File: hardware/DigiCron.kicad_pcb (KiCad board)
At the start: 2 copper layers, 36 x 36 mm, 57 parts, among them J100 Solder pad, J101 Solder pad, J102 Solder pad, J103 Solder pad, J200 Conn_Receptacle_2P, J201 Solder pad, J202 Solder pad, J203 Solder pad, J204 Solder pad, Q100 BSS138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

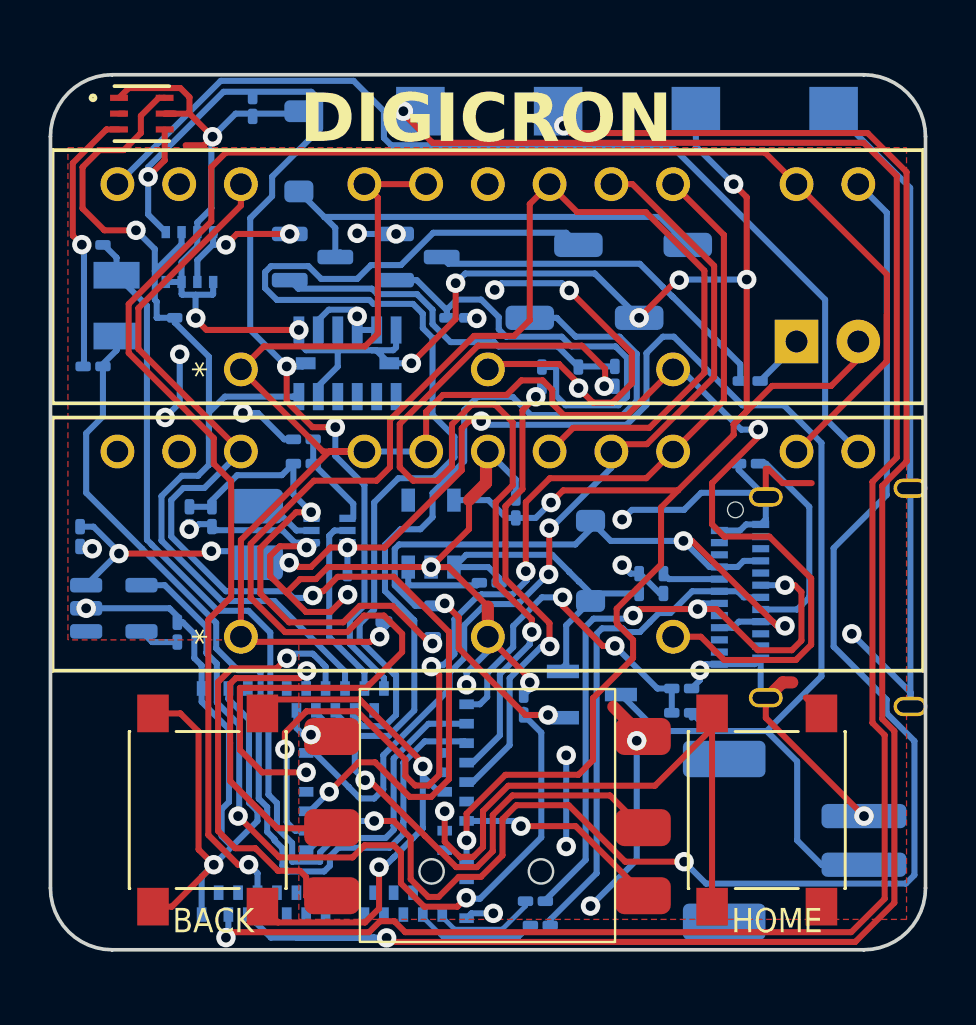
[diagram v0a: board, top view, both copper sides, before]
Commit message: Add mounting tabs to edges of PCB
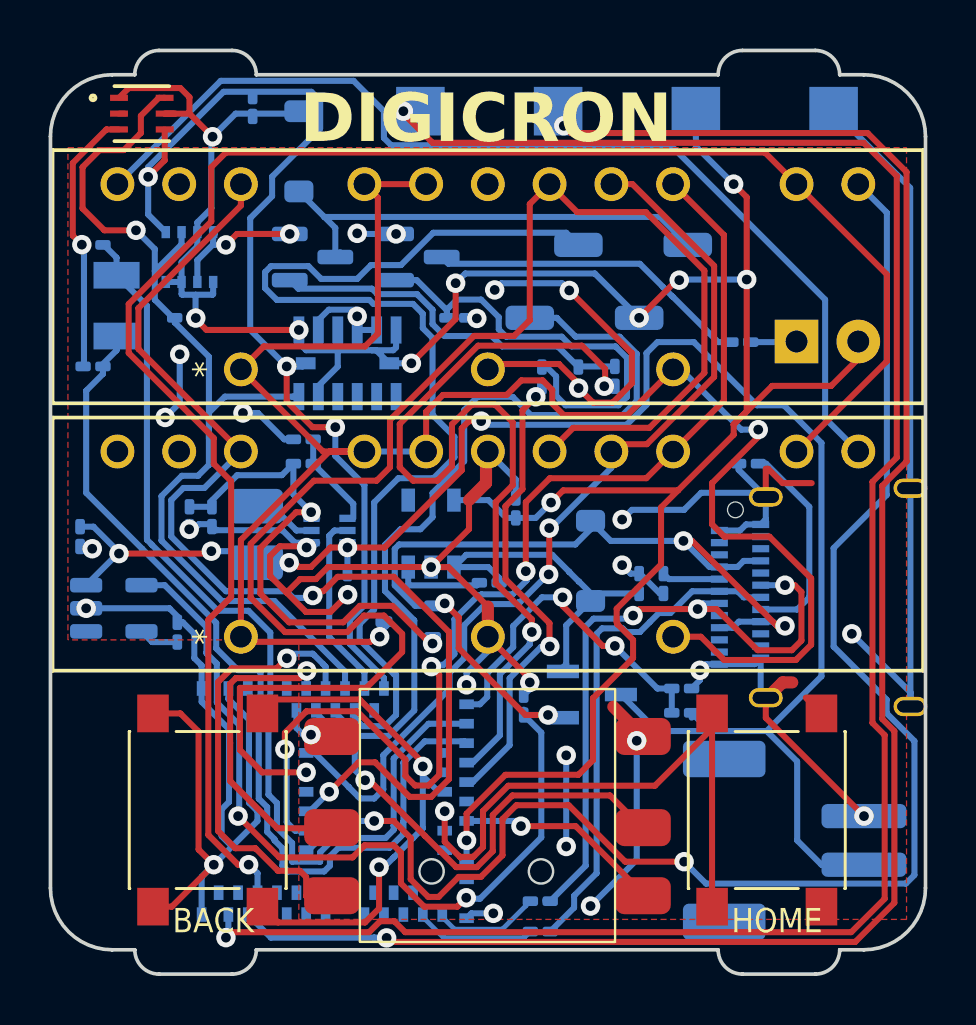
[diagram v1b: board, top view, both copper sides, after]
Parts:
- moved R100 1.65 mm to (208.3, 77.0)
- moved R209 0.25 mm to (200.1, 101.3)
- moved R210 0.20 mm to (200.1, 100.0)
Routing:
- net SWDIO: track 76.5 -> 73.3 mm
- net HCMS_RS: track 75.4 -> 73.4 mm
- net Net-(Q100-D): track 14.8 -> 13.4 mm
- net +3V3: track 109.9 -> 108.7 mm
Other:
- board size 36 x 36 mm -> 36 x 38 mm
- board text added: "V1"

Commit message: Generate Gerber files
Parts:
- moved C200 58.2 mm to (148.8, 105.0)
- moved C202 58.2 mm to (136.8, 105.0)
- moved C203 58.2 mm to (130.3, 102.3)
- moved C205 58.2 mm to (125.8, 103.1)
- moved C206 58.2 mm to (126.3, 91.1)
- moved C207 58.2 mm to (126.3, 96.1)
- moved D100 58.2 mm to (155.3, 95.1)
- moved D101 58.2 mm to (134.8, 87.3)
- moved D200 58.2 mm to (146.8, 104.1)
- moved D201 58.2 mm to (139.3, 106.6)
- moved J100 58.2 mm to (150.8, 91.1)
- moved J101 58.2 mm to (148.8, 94.1)
- moved J102 58.2 mm to (146.3, 91.1)
- moved J103 58.2 mm to (144.3, 94.1)
- moved J200 58.2 mm to (155.2, 115.6)
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
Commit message: Make minor alterations to not use custom font on PCB
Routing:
- net GND: track 192.8 -> 199.8 mm
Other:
- board text removed: "DIGICRON"

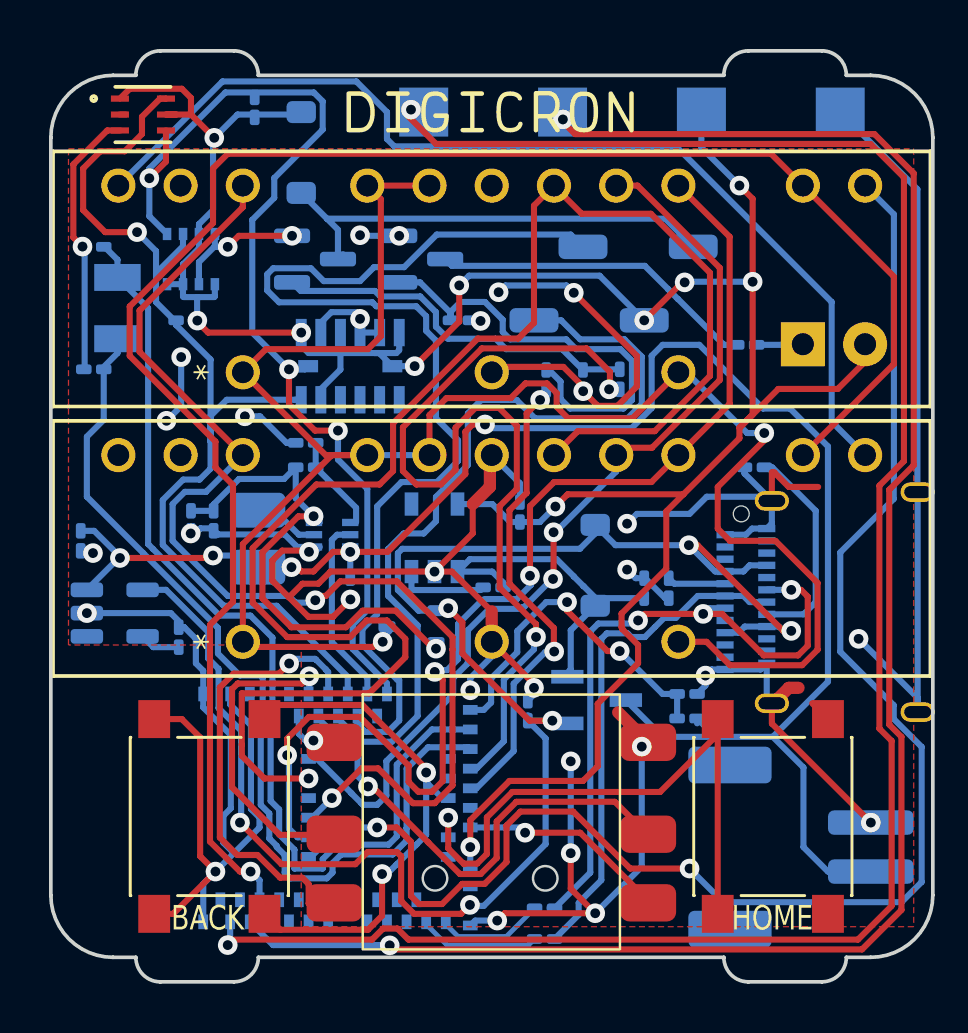
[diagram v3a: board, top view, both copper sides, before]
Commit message: Update PCB to use 0402 resistor/capacitor packages
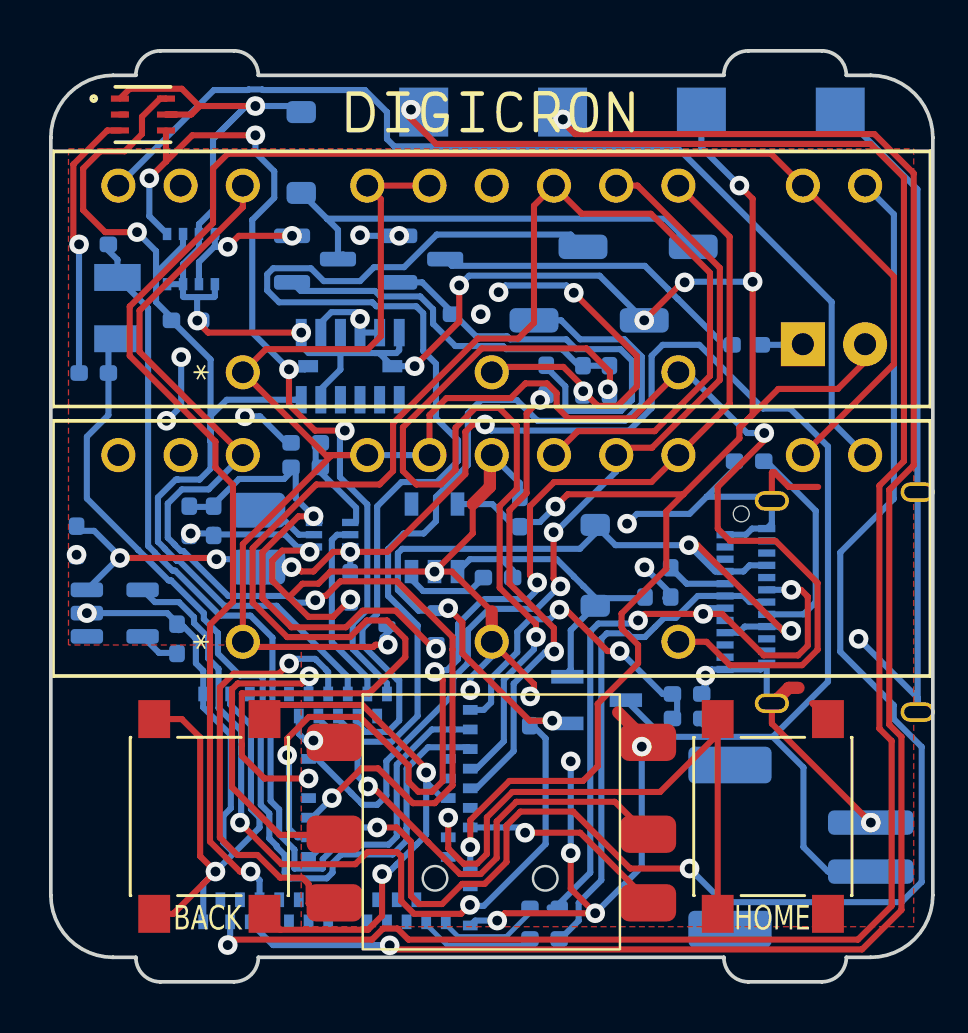
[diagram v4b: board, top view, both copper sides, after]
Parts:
- C200, C201, C202, C203, C204, C205, C206, C207, R100, R101, R102, R103, R104, R106, R107: footprint Capacitor_SMD:C_0201_0603Metric_Pad0.64x0.40mm_HandSolder -> Resistor_SMD:R_0402_1005Metric_Pad0.72x0.64mm_HandSolder
- R200, R201, R202, R203, R204, R205, R206, R207, R208, R209, R210: footprint Resistor_SMD:R_0201_0603Metric_Pad0.64x0.40mm_HandSolder -> Resistor_SMD:R_0402_1005Metric_Pad0.72x0.64mm_HandSolder
- moved R107 0.54 mm to (132.9, 86.0), turned to -90 degrees
- moved R203 0.45 mm to (142.8, 104.6)
- moved R103 0.42 mm to (147.4, 96.6)
- moved R102 0.34 mm to (141.5, 93.9)
- moved R201 0.33 mm to (153.1, 99.9)
- moved R200 0.25 mm to (149.9, 104.8)
- moved C200 0.24 mm to (148.8, 104.8)
- moved C205 0.17 mm to (125.6, 103.1)
- moved C207 0.15 mm to (126.3, 96.3)
- moved C206 0.10 mm to (126.3, 91.0)
- moved R208 0.10 mm to (129.7, 107.1)
- moved R202 0.08 mm to (144.1, 110.1)
- moved C203 0.07 mm to (130.2, 102.3)
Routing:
- net SCL: track 43.4 -> 37.0 mm, vias 3 -> 4
- net +3V3: track 108.7 -> 112.3 mm
- net Net-(D200-K): track 14.6 -> 13.2 mm
- net Net-(Q100-G): track 18.4 -> 17.4 mm
- net HCMS_CLOCK: track 47.2 -> 48.0 mm
- net VBAT: track 70.9 -> 71.4 mm

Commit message: Fix a few resistor values on PCB relating to power management
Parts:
- R205: value 732K -> 100K
- R206: value 100K -> 10K
- R207: value 100K -> 5.1K
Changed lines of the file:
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@@
 			)
 		)
-		(property "Value" "732K"
+		(property "Value" "100K"
 			(at 0 -1.17 0)
 			(layer "B.Fab")
@@
 			)
 		)
-		(property "Value" "100K"
+		(property "Value" "10K"
 			(at 0 -1.17 0)
 			(layer "B.Fab")
@@
 			)
 		)
-		(property "Value" "100K"
+		(property "Value" "5.1K"
 			(at 0 -1.17 180)
 			(layer "B.Fab")

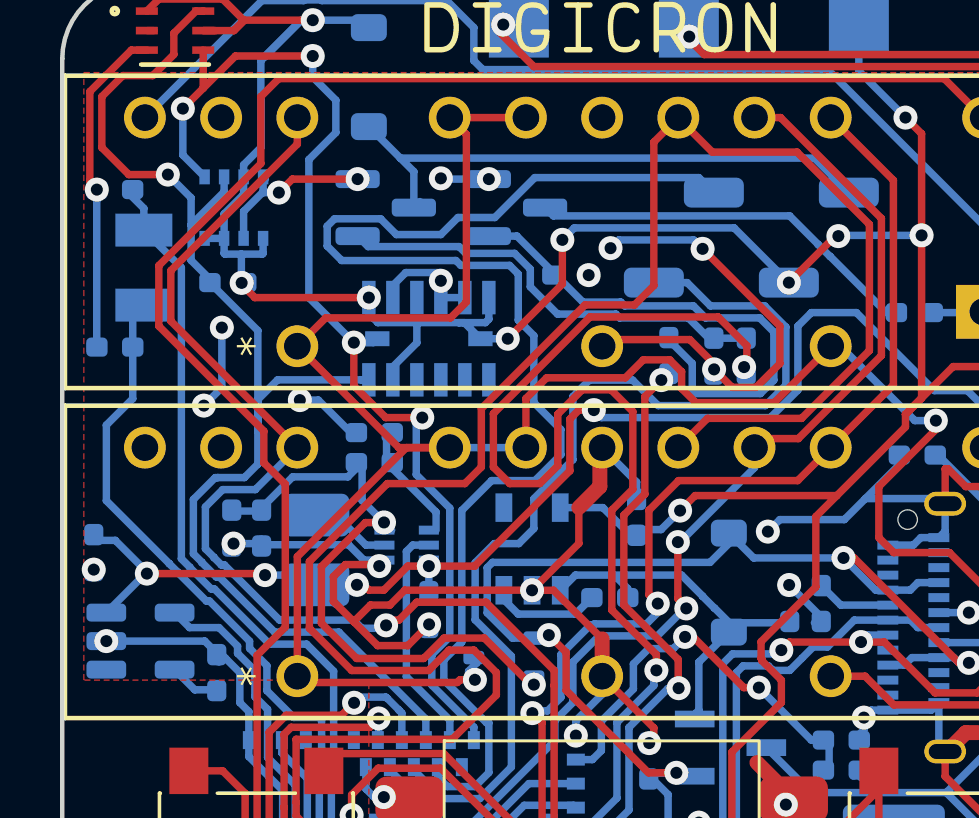
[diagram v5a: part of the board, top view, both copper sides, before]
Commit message: Make a few changes to footprint selection and resistor/capacitor values
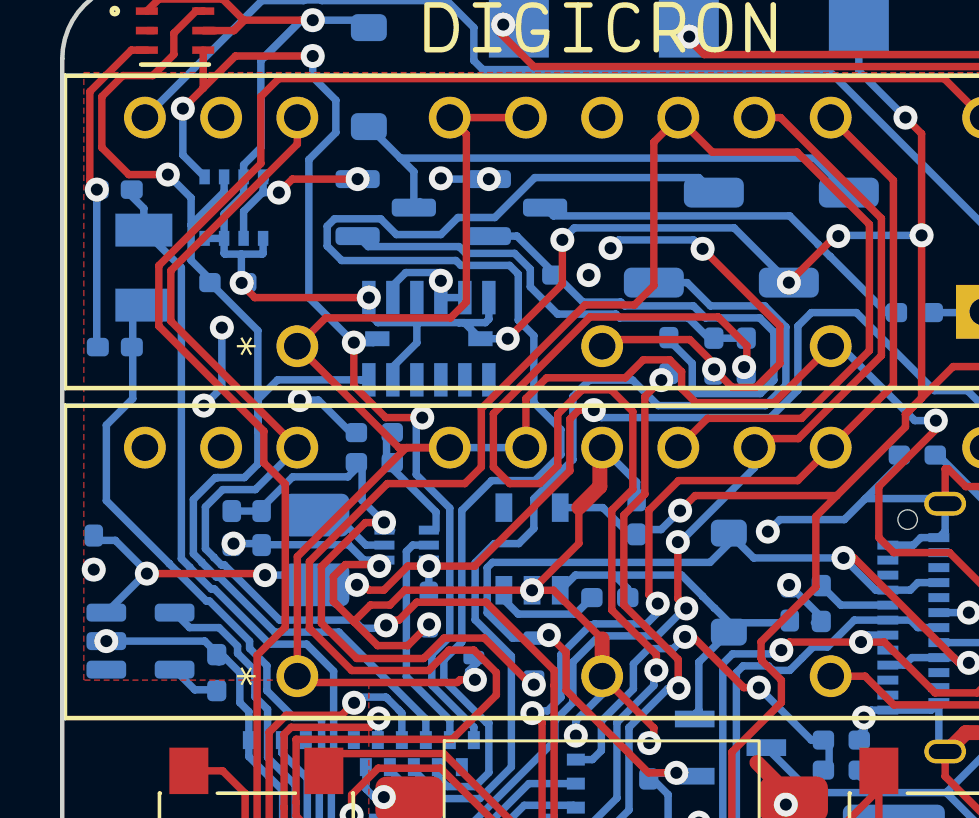
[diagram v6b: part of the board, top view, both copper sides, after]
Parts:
- C200, C201, C202, C203, C204, C205, C206, C207: footprint Resistor_SMD:R_0402_1005Metric_Pad0.72x0.64mm_HandSolder -> Capacitor_SMD:C_0402_1005Metric_Pad0.74x0.62mm_HandSolder
- R206: value 10K -> 1M
- R207: value 5.1K -> 470K
- renumbered U1 to U106

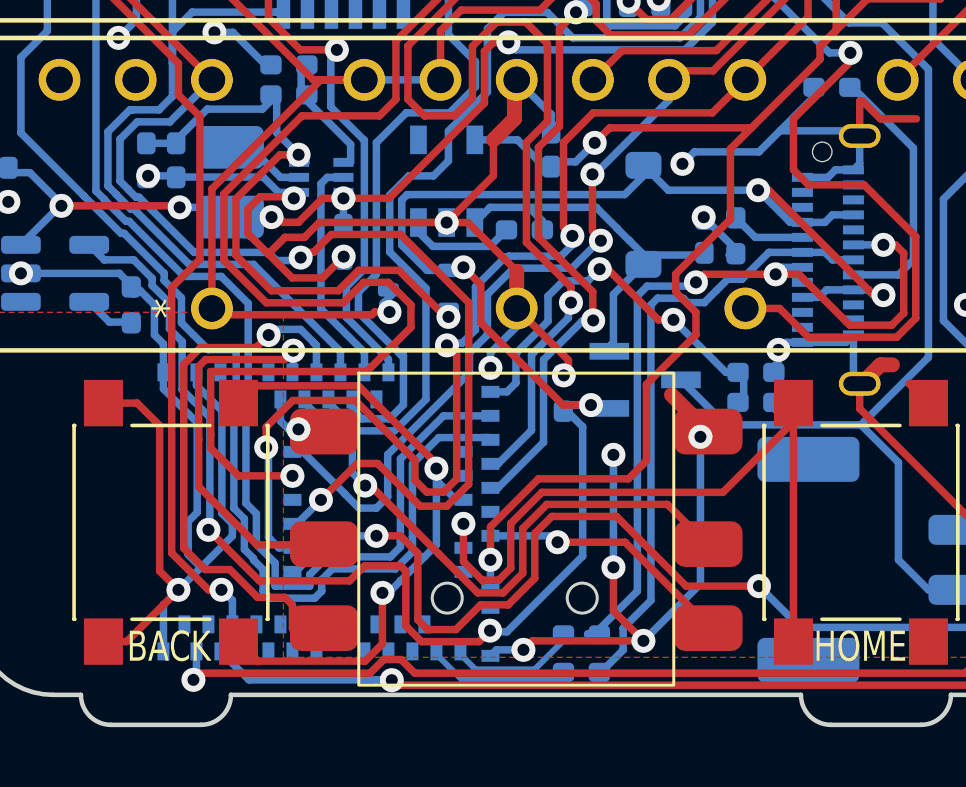
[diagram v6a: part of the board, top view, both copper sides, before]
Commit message: Reroute MCU pins to avoid vias inside pads
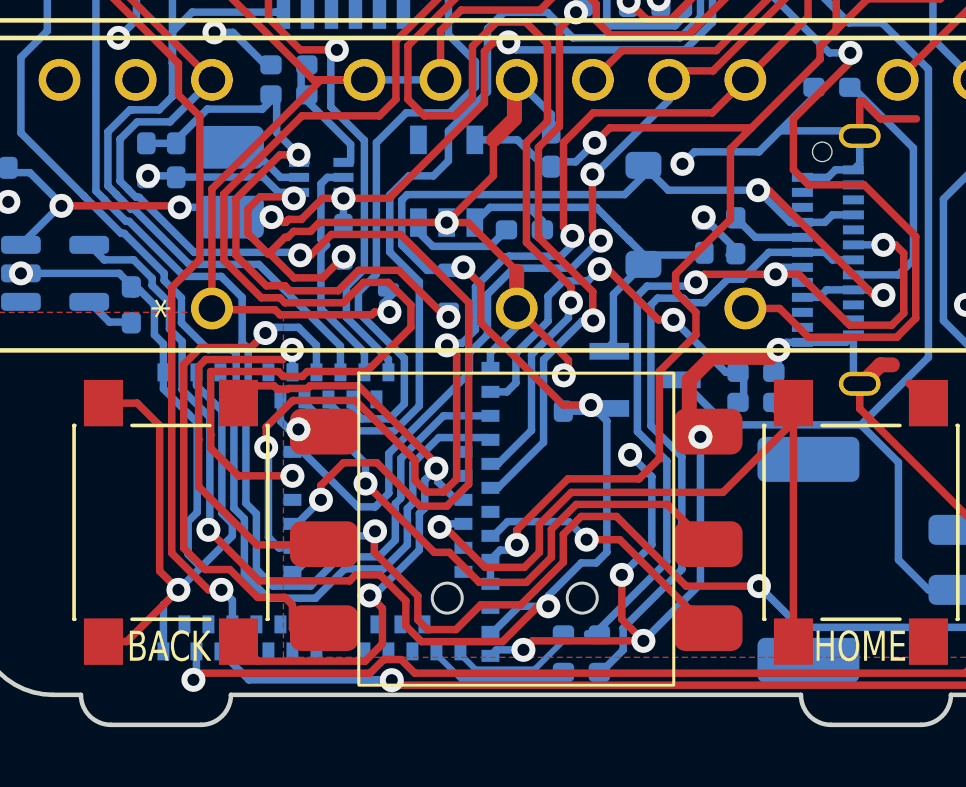
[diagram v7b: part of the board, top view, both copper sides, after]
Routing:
- net GND: track 199.7 -> 203.9 mm, vias 32 -> 31
- net VBUS: track 71.0 -> 73.3 mm
- net Net-(R209-Pad2): track 20.6 -> 21.5 mm
- net Net-(R210-Pad2): track 26.8 -> 27.6 mm
- net JOY_RIGHT: track 19.3 -> 18.6 mm
- net HCMS_DATA_IN: track 63.6 -> 63.0 mm

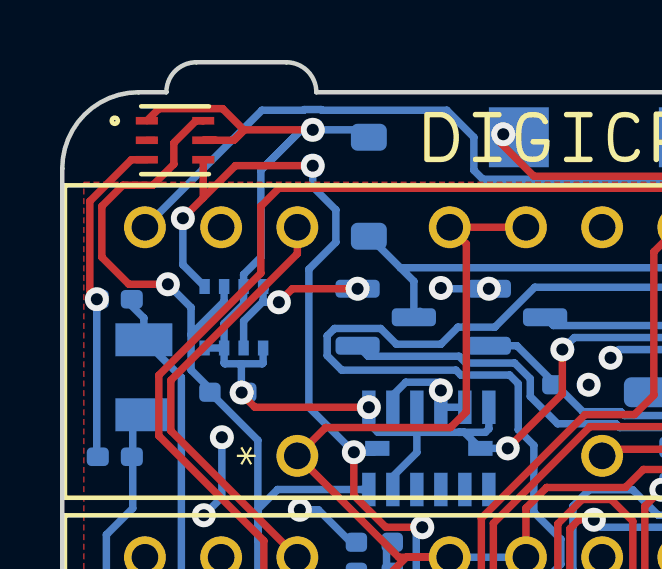
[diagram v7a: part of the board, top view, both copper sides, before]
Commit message: Remove LTR-390 to make assembly easier
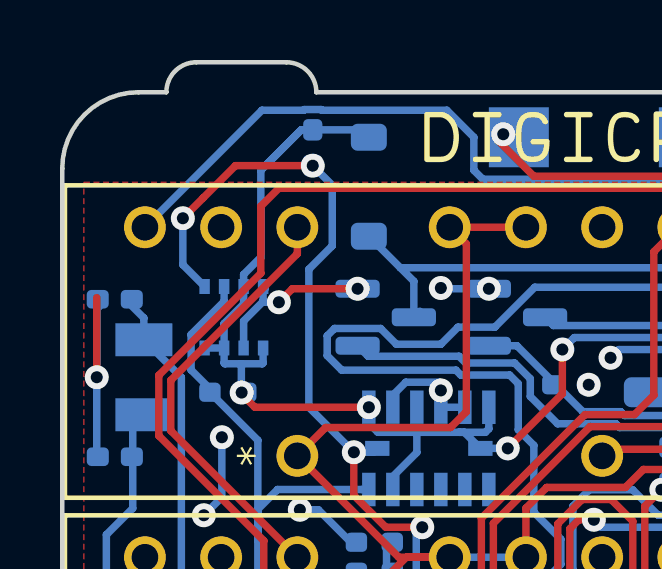
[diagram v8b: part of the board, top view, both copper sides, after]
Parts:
- removed U106: LTR-390UV-01, LTR390:SMD6_LTR-390UV-01_LTO
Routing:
- net SDA: track 42.7 -> 31.5 mm, vias 1 -> 0
- net +3V3: track 112.2 -> 103.8 mm, vias 11 -> 10
- net GND: track 203.9 -> 200.7 mm
- net SCL: track 37.0 -> 35.7 mm
